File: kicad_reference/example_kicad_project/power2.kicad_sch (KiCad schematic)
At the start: 2 parts

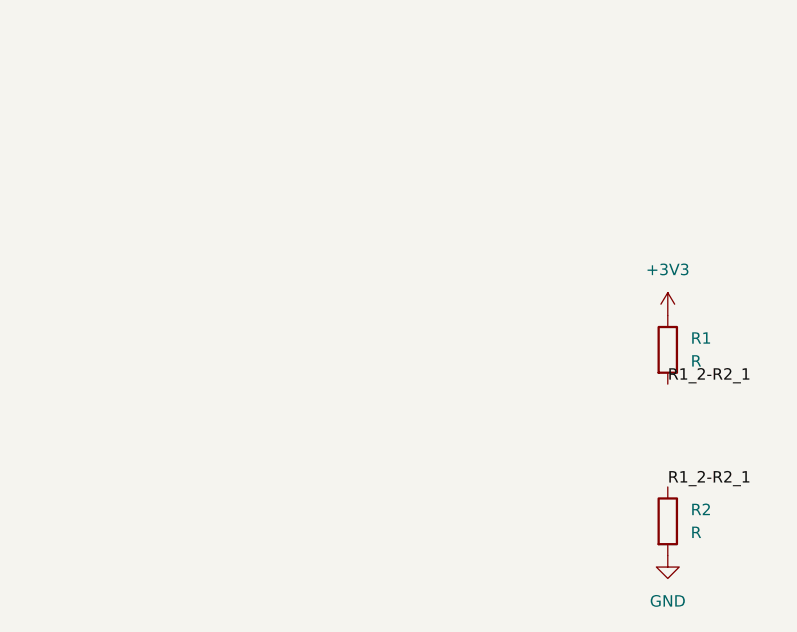
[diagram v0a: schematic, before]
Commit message: modified example to be hierarchical. add kicad_to_skidl script
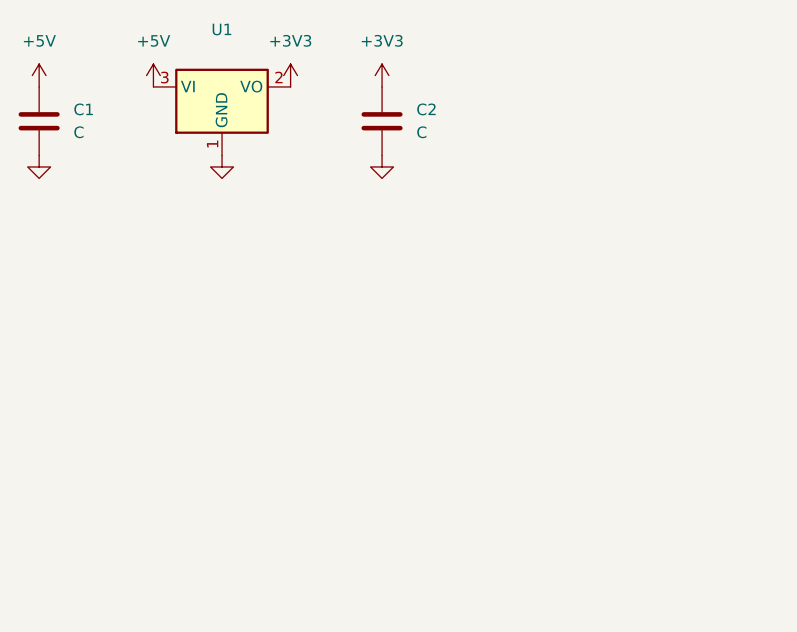
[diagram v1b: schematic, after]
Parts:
- removed R1, R2: R, symbol Device:R
- added C1, C2: C, Capacitor_SMD:C_0603_1608Metric, symbol Device:C
- added U1: NCP1117-3.3_SOT223, Package_TO_SOT_SMD:SOT-223-3_TabPin2, symbol Regulator_Linear:NCP1117-3.3_SOT223
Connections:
- net +3V3: now also C2.1, U1.2 (VO)
- net GND: now also C1.2, C2.2, U1.1 (GND)
- new net +5V: C1.1, U1.3 (VI)
